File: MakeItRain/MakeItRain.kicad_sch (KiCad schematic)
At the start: 15 parts, among them IC1 MCP23008T-E_SS, J1 Conn_02x15_Odd_Even, J2 Conn_02x19_Odd_Even, J3 Conn_01x19

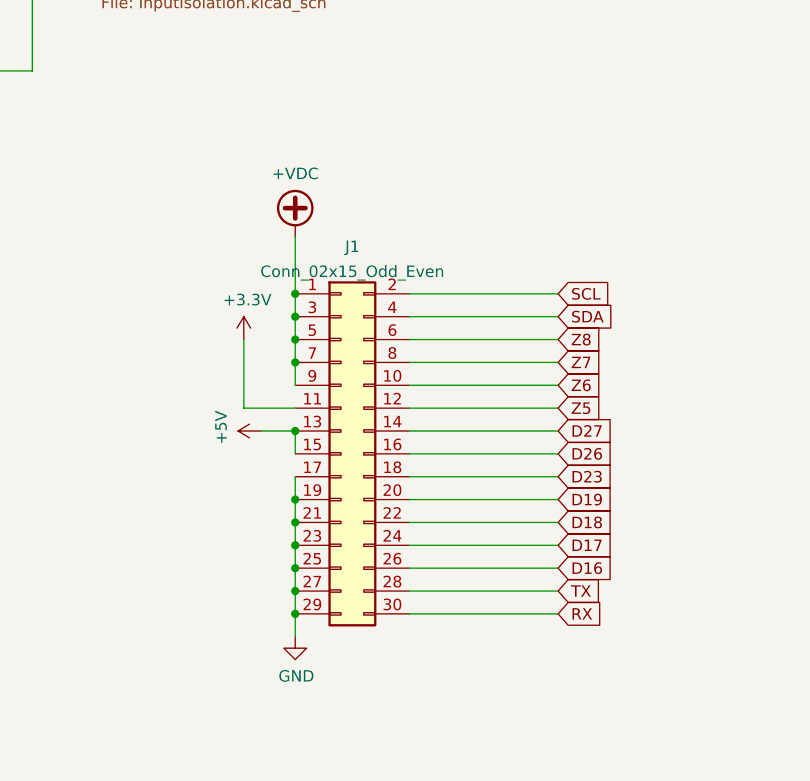
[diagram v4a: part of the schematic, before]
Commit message: replacing the daughterboard plug
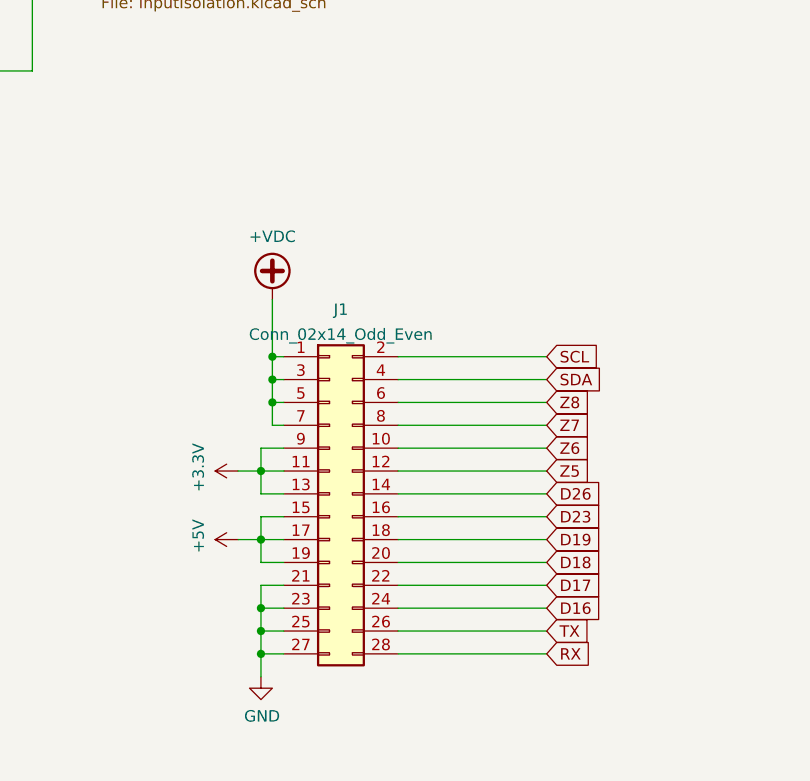
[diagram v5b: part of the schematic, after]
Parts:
- removed J1: Conn_02x15_Odd_Even, Connector_PinHeader_2.54mm:PinHeader_2x15_P2.54mm_Vertical, symbol Connector_Generic:Conn_02x15_Odd_Even
- added J1: Conn_02x14_Odd_Even, Connector_PinHeader_2.54mm:PinHeader_2x14_P2.54mm_Vertical, symbol Connector_Generic:Conn_02x14_Odd_Even
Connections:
- net +3V3: now also J1.11 (Pin_11), J1.13 (Pin_13), J1.9 (Pin_9)
- net +5V: now also J1.15 (Pin_15), J1.17 (Pin_17), J1.19 (Pin_19)
- net +VDC: now also J1.1 (Pin_1), J1.3 (Pin_3), J1.5 (Pin_5), J1.7 (Pin_7)
- net D16: now also J1.24 (Pin_24)
- net D17: now also J1.22 (Pin_22)
- net D18: now also J1.20 (Pin_20)
- net D19: now also J1.18 (Pin_18)
- net D21: now also J1.4 (Pin_4)
- net D22: now also J1.2 (Pin_2)
- net D23: now also J1.16 (Pin_16)
- net D26: now also J1.14 (Pin_14)
- net GND: now also J1.21 (Pin_21), J1.23 (Pin_23), J1.25 (Pin_25), J1.27 (Pin_27)
- net RX: now also J1.28 (Pin_28)
- net TX: now also J1.26 (Pin_26)
- net Z5: now also J1.12 (Pin_12)
- net Z6: now also J1.10 (Pin_10)
- net Z7: now also J1.8 (Pin_8)
- net Z8: now also J1.6 (Pin_6)

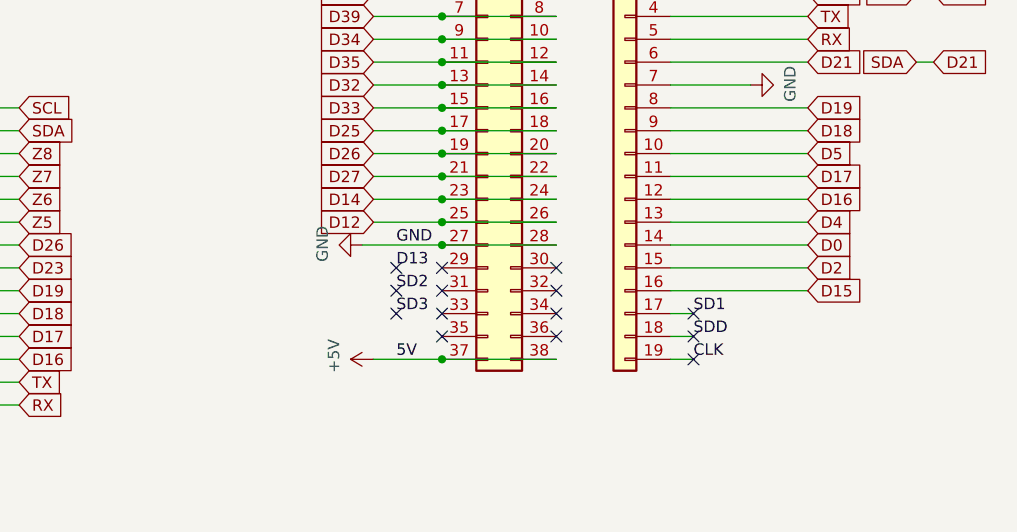
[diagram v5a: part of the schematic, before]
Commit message: working on getting the test code for the MCP23008 into the fw. working on the pins and getting all of that stuff placed on the PCB.
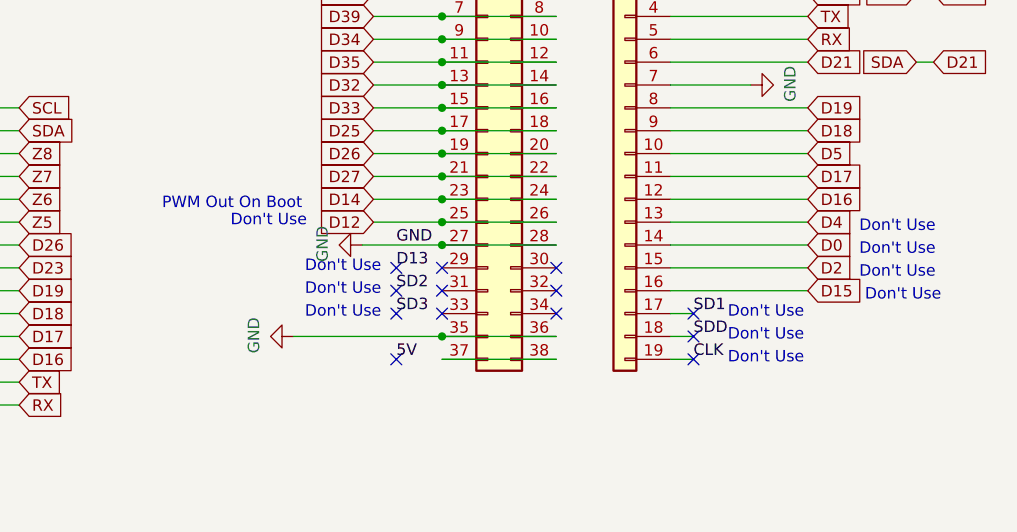
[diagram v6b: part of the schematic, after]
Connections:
- net +5V: no longer J2.37 (Pin_37), J2.38 (Pin_38)
- net GND: now also J2.35 (Pin_35), J2.36 (Pin_36)
- new net: J2.37 (Pin_37), J2.38 (Pin_38)
- no-connect marks 19 -> 18
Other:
- note added: "Don't Use"
- note added: "PWM Out On Boot"
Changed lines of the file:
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@@
 (kicad_sch (version 20211123) (generator eeschema)
   (paper "A4")
+  (junction (at 220.98 146.05) (diameter 0) (color 0 0 0 0)
+  )
+  (junction (at 220.98 130.81) (diameter 0) (color 0 0 0 0)
+  )
+  (junction (at 143.51 120.65) (diameter 0) (color 0 0 0 0)
+  )
+  (junction (at 220.98 110.49) (diameter 0) (color 0 0 0 0)
+  )
+  (junction (at 220.98 115.57) (diameter 0) (color 0 0 0 0)
+  )
+  (junction (at 220.98 118.11) (diameter 0) (color 0 0 0 0)
+  )
   (junction (at 220.98 135.89) (diameter 0) (color 0 0 0 0)
   )
-  (junction (at 220.98 130.81) (diameter 0) (color 0 0 0 0)
-  )
-  (junction (at 143.51 120.65) (diameter 0) (color 0 0 0 0)
-  )
-  (junction (at 220.98 110.49) (diameter 0) (color 0 0 0 0)
-  )
-  (junction (at 220.98 115.57) (diameter 0) (color 0 0 0 0)
-  )
-  (junction (at 220.98 118.11) (diameter 0) (color 0 0 0 0)
-  )
   (junction (at 48.895 155.575) (diameter 0) (color 0 0 0 0)
   )
@@
   )
   (junction (at 48.895 145.415) (diameter 0) (color 0 0 0 0)
-  )
-  (junction (at 220.98 148.59) (diameter 0) (color 0 0 0 0)
   )
   (junction (at 53.34 135.255) (diameter 0) (color 0 0 0 0)
@@
   (no_connect (at 58.42 158.115))
   (no_connect (at 91.44 158.115))
+  (no_connect (at 215.9 148.59))
   (no_connect (at 194.31 43.815))
   (no_connect (at 194.31 46.355))
   (no_connect (at 58.42 153.035))
-  (no_connect (at 220.98 146.05))
   (no_connect (at 215.9 143.51))
   (no_connect (at 215.9 140.97))
@@
   (no_connect (at 233.68 140.97))
   (no_connect (at 233.68 143.51))
-  (no_connect (at 233.68 146.05))
   (no_connect (at 248.92 148.59))
   (wire (pts (xy 91.44 155.575) (xy 93.98 155.575))
@@
     (stroke (width 0) (type default) (color 0 0 0 0))
   )
+  (wire (pts (xy 220.98 146.05) (xy 233.68 146.05))
+    (stroke (width 0) (type default) (color 0 0 0 0))
+  )
   (wire (pts (xy 91.44 137.795) (xy 93.98 137.795))
     (stroke (width 0) (type default) (color 0 0 0 0))
@@
     (stroke (width 0) (type default) (color 0 0 0 0))
   )
-  (wire (pts (xy 233.68 135.89) (xy 220.98 135.89))
+  (wire (pts (xy 204.47 146.05) (xy 220.98 146.05))
     (stroke (width 0) (type default) (color 0 0 0 0))
   )
@@
     (stroke (width 0) (type default) (color 0 0 0 0))
   )
+  (wire (pts (xy 220.98 148.59) (xy 233.68 148.59))
+    (stroke (width 0) (type default) (color 0 0 0 0))
+  )
+  (wire (pts (xy 212.09 135.89) (xy 220.98 135.89))
+    (stroke (width 0) (type default) (color 0 0 0 0))
+  )
   (wire (pts (xy 213.36 128.27) (xy 220.98 128.27))
     (stroke (width 0) (type default) (color 0 0 0 0))
@@
     (stroke (width 0) (type default) (color 0 0 0 0))
   )
-  (wire (pts (xy 212.09 135.89) (xy 220.98 135.89))
-    (stroke (width 0) (type default) (color 0 0 0 0))
-  )
   (wire (pts (xy 246.38 102.87) (xy 255.27 102.87))
     (stroke (width 0) (type default) (color 0 0 0 0))
@@
     (stroke (width 0) (type default) (color 0 0 0 0))
   )
-  (wire (pts (xy 213.36 148.59) (xy 220.98 148.59))
-    (stroke (width 0) (type default) (color 0 0 0 0))
-  )
   (wire (pts (xy 233.68 115.57) (xy 220.98 115.57))
     (stroke (width 0) (type default) (color 0 0 0 0))
@@
     (stroke (width 0) (type default) (color 0 0 0 0))
   )
-  (wire (pts (xy 233.68 148.59) (xy 220.98 148.59))
-    (stroke (width 0) (type default) (color 0 0 0 0))
-  )
   (wire (pts (xy 116.84 77.47) (xy 116.84 88.9))
     (stroke (width 0) (type default) (color 0 0 0 0))
@@
     (stroke (width 0) (type default) (color 0 0 0 0))
   )
+  (wire (pts (xy 220.98 135.89) (xy 233.68 135.89))
+    (stroke (width 0) (type default) (color 0 0 0 0))
+  )
   (wire (pts (xy 246.38 130.81) (xy 261.62 130.81))
     (stroke (width 0) (type default) (color 0 0 0 0))
@@
   (wire (pts (xy 233.68 113.03) (xy 220.98 113.03))
     (stroke (width 0) (type default) (color 0 0 0 0))
+  )
+  (text "Don't Use" (at 205.74 139.065 0)
+    (effects (font (size 1.27 1.27)) (justify left bottom))
+  )
+  (text "Don't Use" (at 267.335 134.62 0)
+    (effects (font (size 1.27 1.27)) (justify left bottom))
+  )
+  (text "Don't Use" (at 252.73 144.145 0)
+    (effects (font (size 1.27 1.27)) (justify left bottom))
+  )
+  (text "Don't Use" (at 267.97 142.24 0)
+    (effects (font (size 1.27 1.27)) (justify left bottom))
+  )
+  (text "Don't Use" (at 205.74 141.605 0)
+    (effects (font (size 1.27 1.27)) (justify left bottom))
+  )
+  (text "Don't Use" (at 252.73 146.685 0)
+    (effects (font (size 1.27 1.27)) (justify left bottom))
+  )
+  (text "Don't Use" (at 205.74 144.145 0)
+    (effects (font (size 1.27 1.27)) (justify left bottom))
+  )
+  (text "Don't Use" (at 252.73 149.225 0)
+    (effects (font (size 1.27 1.27)) (justify left bottom))
+  )
+  (text "Don't Use" (at 267.335 139.7 0)
+    (effects (font (size 1.27 1.27)) (justify left bottom))
+  )
+  (text "PWM Out On Boot" (at 189.865 132.08 0)
+    (effects (font (size 1.27 1.27)) (justify left bottom))
+  )
+  (text "Don't Use" (at 197.485 133.985 0)
+    (effects (font (size 1.27 1.27)) (justify left bottom))
+  )
+  (text "Don't Use" (at 267.335 137.16 0)
+    (effects (font (size 1.27 1.27)) (justify left bottom))
   )
   (label "D13" (at 215.9 138.43 0)
@@
     (pin "1")
   )
-  (symbol (lib_id "power:+5V") (at 213.36 148.59 90) (unit 1)
-    (in_bom yes) (on_board yes)
-    (property "Reference" "#PWR016" (id 0) (at 217.17 148.59 0)
-      (effects (font (size 1.27 1.27)) hide)
-    )
-    (property "Value" "+5V" (id 1) (at 208.9658 148.209 0))
-    (property "Footprint" "" (id 2) (at 213.36 148.59 0)
-      (effects (font (size 1.27 1.27)) hide)
-    )
-    (property "Datasheet" "" (id 3) (at 213.36 148.59 0)
-      (effects (font (size 1.27 1.27)) hide)
-    )
-    (pin "1")
-  )
   (symbol (lib_id "Device:R") (at 53.34 129.54 0) (unit 1)
     (in_bom yes) (on_board yes)
@@
   (symbol (lib_id "power:+5V") (at 139.7 140.97 90) (unit 1)
     (in_bom yes) (on_board yes)
-    (property "Reference" "#PWR?" (id 0) (at 143.51 140.97 0)
+    (property "Reference" "#PWR0105" (id 0) (at 143.51 140.97 0)
       (effects (font (size 1.27 1.27)) hide)
     )
@@
     (pin "1")
   )
+  (symbol (lib_id "power:GND") (at 204.47 146.05 270) (mirror x) (unit 1)
+    (in_bom yes) (on_board yes)
+    (property "Reference" "#PWR0103" (id 0) (at 198.12 146.05 0)
+      (effects (font (size 1.27 1.27)) hide)
+    )
+    (property "Value" "GND" (id 1) (at 200.0758 145.923 0))
+    (property "Footprint" "" (id 2) (at 204.47 146.05 0)
+      (effects (font (size 1.27 1.27)) hide)
+    )
+    (property "Datasheet" "" (id 3) (at 204.47 146.05 0)
+      (effects (font (size 1.27 1.27)) hide)
+    )
+    (pin "1")
+  )
   (symbol (lib_id "Device:R") (at 36.83 129.54 0) (unit 1)
     (in_bom yes) (on_board yes)
@@
   (symbol (lib_id "power:GND") (at 142.24 156.21 0) (unit 1)
     (in_bom yes) (on_board yes)
-    (property "Reference" "#PWR?" (id 0) (at 142.24 162.56 0)
+    (property "Reference" "#PWR0104" (id 0) (at 142.24 162.56 0)
       (effects (font (size 1.27 1.27)) hide)
     )
@@
   (symbol (lib_id "power:+3.3V") (at 139.7 133.35 90) (unit 1)
     (in_bom yes) (on_board yes)
-    (property "Reference" "#PWR?" (id 0) (at 143.51 133.35 0)
+    (property "Reference" "#PWR0106" (id 0) (at 143.51 133.35 0)
       (effects (font (size 1.27 1.27)) hide)
     )
@@
   (symbol (lib_id "power:+VDC") (at 143.51 114.3 0) (unit 1)
     (in_bom yes) (on_board yes)
-    (property "Reference" "#PWR?" (id 0) (at 143.51 116.84 0)
+    (property "Reference" "#PWR0107" (id 0) (at 143.51 116.84 0)
       (effects (font (size 1.27 1.27)) hide)
     )
@@
       (reference "#PWR015") (unit 1) (value "GND") (footprint "")
     )
-    (path "/00000000-0000-0000-0000-0000617c717d"
-      (reference "#PWR016") (unit 1) (value "+5V") (footprint "")
-    )
     (path "/3671feff-f38f-4911-9d81-62ea1ed2e827"
       (reference "#PWR017") (unit 1) (value "+3.3V") (footprint "")
@@
       (reference "#PWR0102") (unit 1) (value "+3.3V") (footprint "")
     )
+    (path "/45143e3f-fce8-46ca-878b-622ef7f7645d"
+      (reference "#PWR0103") (unit 1) (value "GND") (footprint "")
+    )
+    (path "/681cdba4-7e5c-45e3-bb80-441c833d63d5"
+      (reference "#PWR0104") (unit 1) (value "GND") (footprint "")
+    )
     (path "/105ec9f9-b3cb-4791-8471-0b07955c75c3"
-      (reference "#PWR?") (unit 1) (value "+5V") (footprint "")
-    )
-    (path "/681cdba4-7e5c-45e3-bb80-441c833d63d5"
-      (reference "#PWR?") (unit 1) (value "GND") (footprint "")
+      (reference "#PWR0105") (unit 1) (value "+5V") (footprint "")
     )
     (path "/a7c33a02-d62e-4894-b5f3-375513d31e41"
-      (reference "#PWR?") (unit 1) (value "+3.3V") (footprint "")
+      (reference "#PWR0106") (unit 1) (value "+3.3V") (footprint "")
     )
     (path "/e6888b19-70c1-4772-9216-b3b53946bc0a"
-      (reference "#PWR?") (unit 1) (value "+VDC") (footprint "")
+      (reference "#PWR0107") (unit 1) (value "+VDC") (footprint "")
     )
     (path "/00000000-0000-0000-0000-000061506093/00000000-0000-0000-0000-00006194d07b"

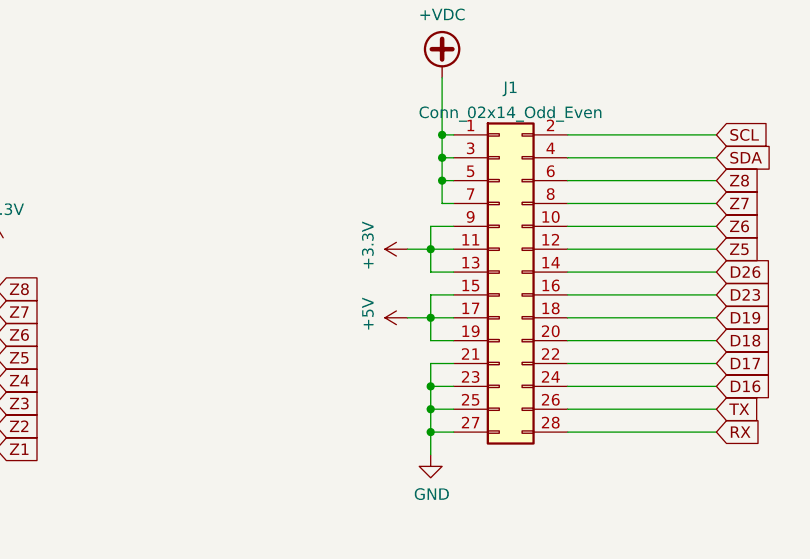
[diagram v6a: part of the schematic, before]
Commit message: removed the 5V on the baseboard and daughterboard plug.
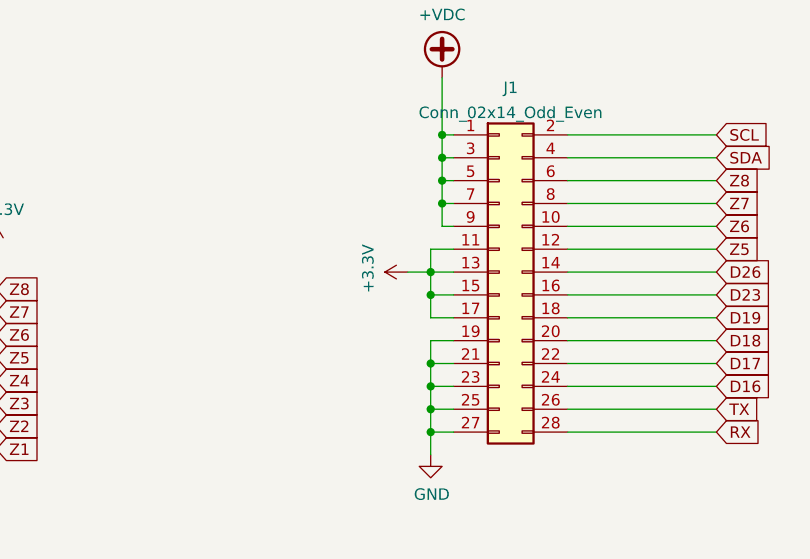
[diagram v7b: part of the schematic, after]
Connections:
- net +3V3: now also J1.15 (Pin_15), J1.17 (Pin_17); no longer J1.9 (Pin_9)
- net +VDC: now also J1.9 (Pin_9)
- net GND: now also J1.19 (Pin_19)
- removed net +5V: J1.15 (Pin_15), J1.17 (Pin_17), J1.19 (Pin_19)
